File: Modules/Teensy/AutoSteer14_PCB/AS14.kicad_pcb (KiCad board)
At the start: 2 copper layers, 159 x 159 mm, 97 parts, among them IC1 AZ1117, IC2 XL2596, IC3 PCA9306DCUR, J1 Motor 2, J10 Teensy_Ethernet, J11 ADS1115, J12 Conn_01x15_Female, J13 Conn_01x08_Female, J14 Conn_01x15_Female, J15 Conn_01x08_Female, J16 SCL, J17 SDA, J18 I2C-3V3, J19 I2C-3V3, J2 Motor 2, J20 ArduSimple_tl, J21 ArduSimple_bl, J22 WemosD1_right, J23 BNO080_left, J24 WemosD1_left, J25 BNO080_right, J26 ArduSimple_tr, J27 ArduSimple_br, J28 DT13-12PA, J3 Motor 1, J4 Motor 1, J5 USB_A, J6 Teensy_USBhost, J7 DT13-12PA, J8 5V Power, J9 HR911105A, K1 SRD-05VDC-SL-C, M1 CMPS14, Q1 BC847, U1 TB6612FNG, U2 SP3485EN-L/TR, U3 PC817X2CSP9F, U4 PC817X2CSP9F, U5 PC817X2CSP9F, U6 PC817X2CSP9F, U7 ACS712ELCTR-05B-T

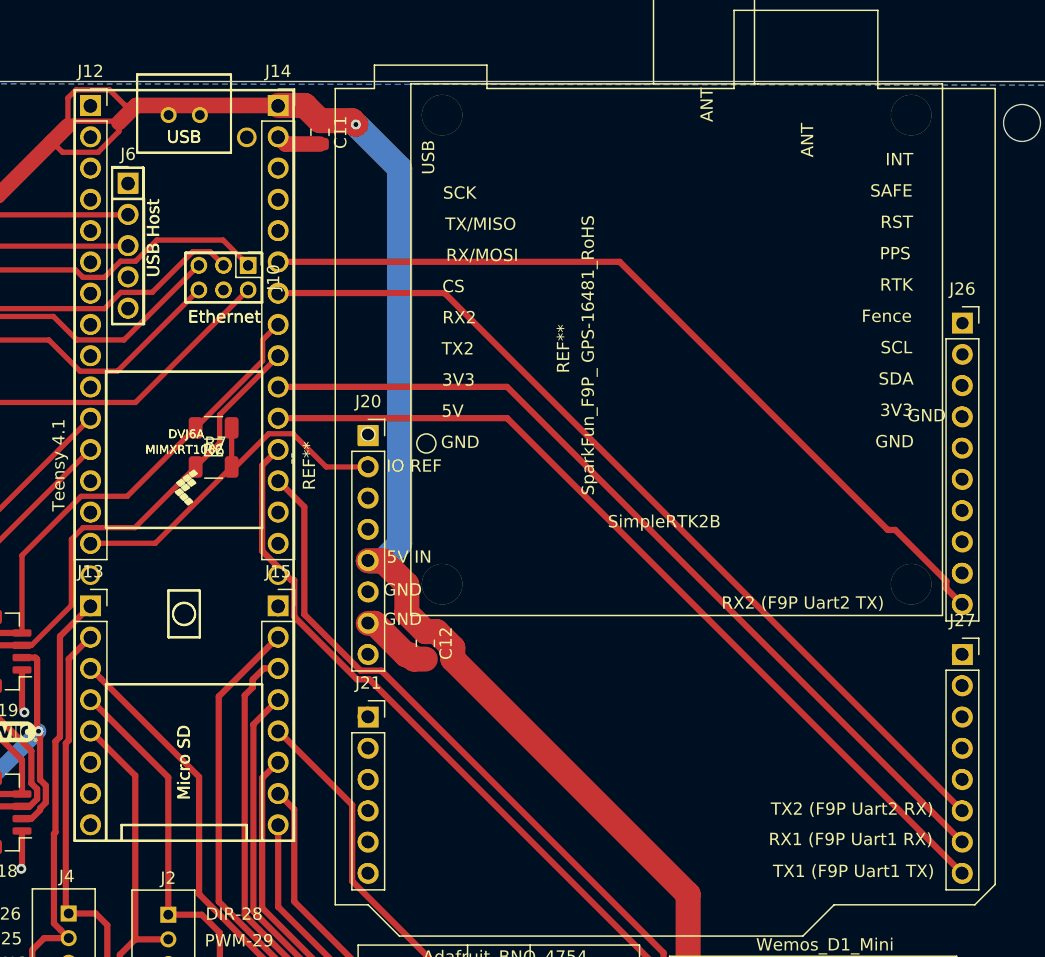
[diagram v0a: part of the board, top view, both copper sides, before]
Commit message: remove 3d models
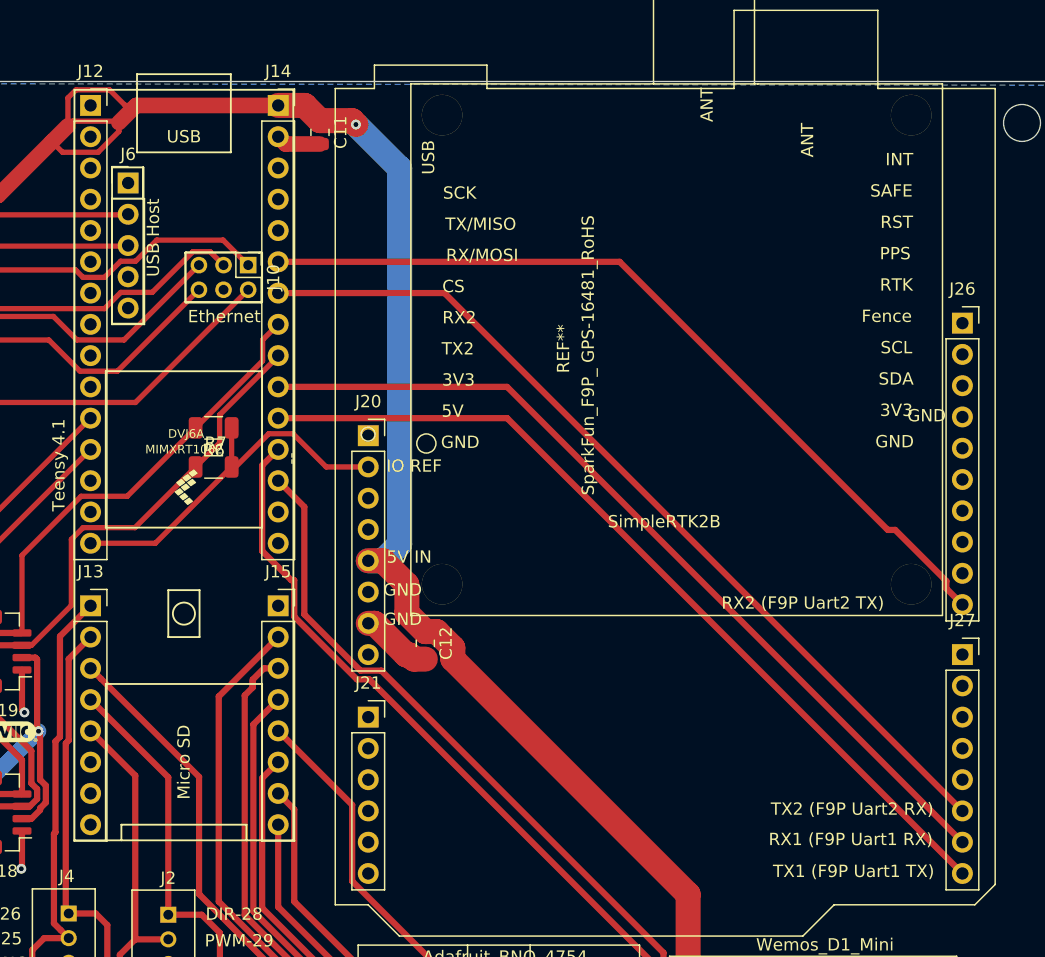
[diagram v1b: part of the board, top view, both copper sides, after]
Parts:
- removed the REF** at (122.5, 48.7)
- removed the REF** at (100.0, 22.0)
